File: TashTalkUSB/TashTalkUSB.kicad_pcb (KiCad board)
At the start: 2 copper layers, 60 x 25 mm, 35 parts, among them J1 TC2030, J3 USB_C_Receptacle_USB2.0_14P, U1 CP2102N-Axx-xQFN20, U2 PIC12F1840-xSN, U3 SN65HVD1473DGSR

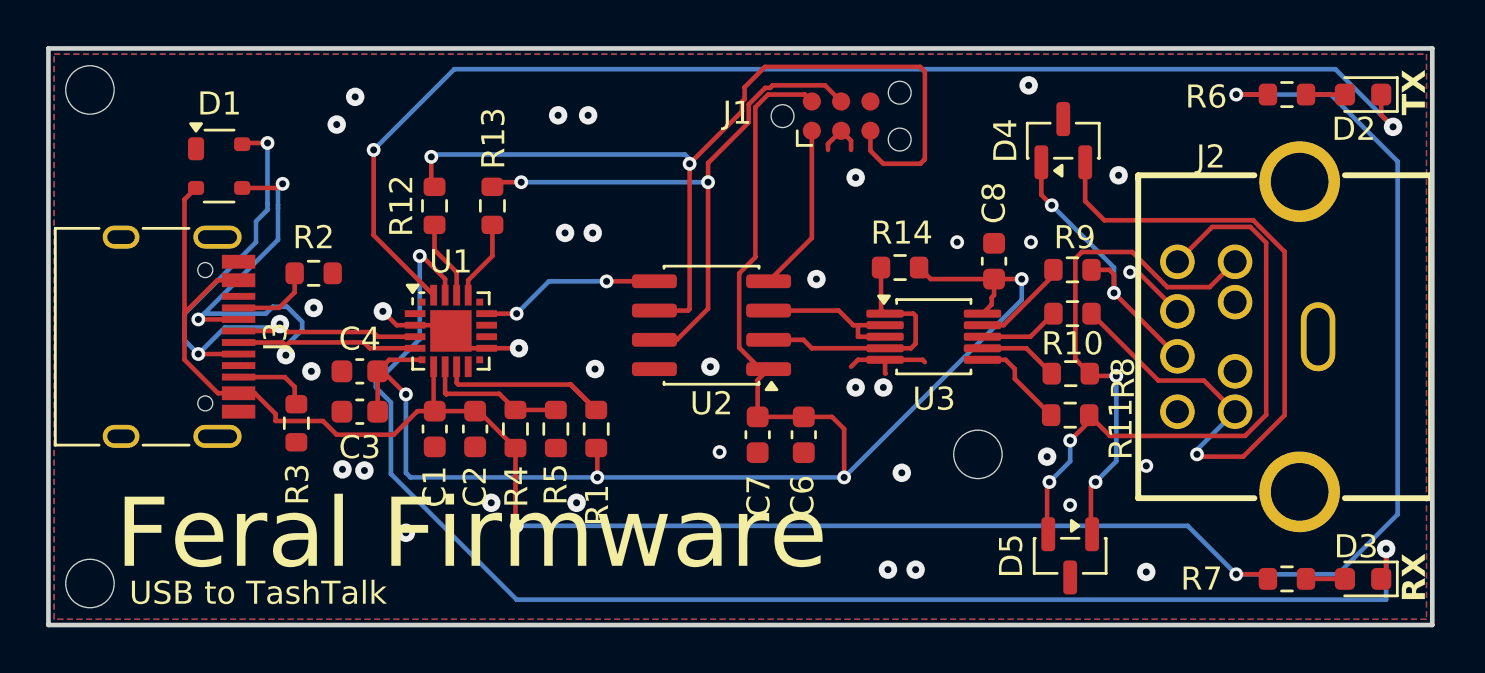
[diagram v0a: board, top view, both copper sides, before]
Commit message: Fix InkTalk and TashTalk USB flipped DIN pins
I accidentally transposed DIN7 and DIN8 when wiring up the connector
in KiCAD (yay weird pin choices on connectors). This explains the rather
odd and unexplainable cases of TashTalk USB not liking resistor pins
on PhoneNET connectors and long cables. It additionally caused InkTalk
to not work at all with the Colour StyleWriter 2200.

Easy fix thankfullly - commit contains just that flip around and some
minor board clean up for the first production-ish run of InkTalk.
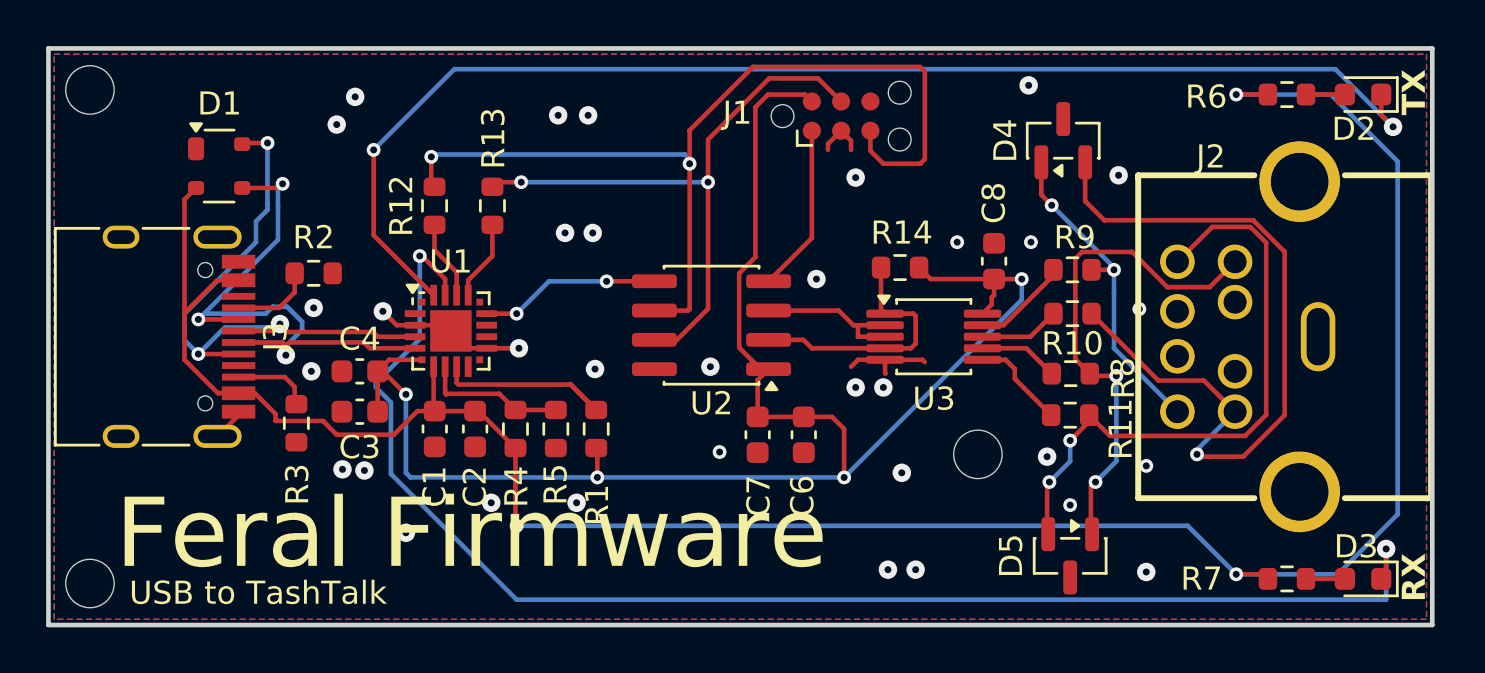
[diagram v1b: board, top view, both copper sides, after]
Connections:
- J2 pad 6: DIN7 -> A
- J2 pad 7: A -> DIN7
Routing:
- net A: track 12.7 -> 14.2 mm
- net GND: track 15.7 -> 14.3 mm
